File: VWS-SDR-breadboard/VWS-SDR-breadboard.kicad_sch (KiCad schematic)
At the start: 86 parts, among them J1 RF_IN, J3 Conn_01x14, U1 GALI-S66, U2 74CBTLV3253DR, U3 MC33078, U4 MC33078, U5 AMS1117-3.3

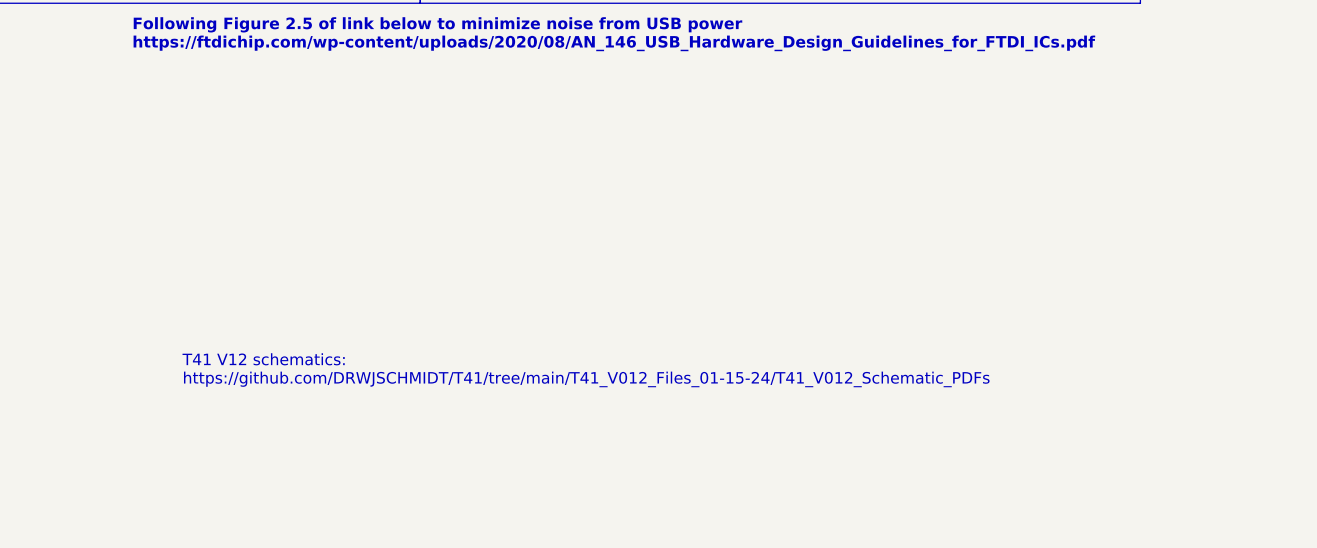
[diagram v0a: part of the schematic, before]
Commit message: Board cleanup; Updated schematic info block
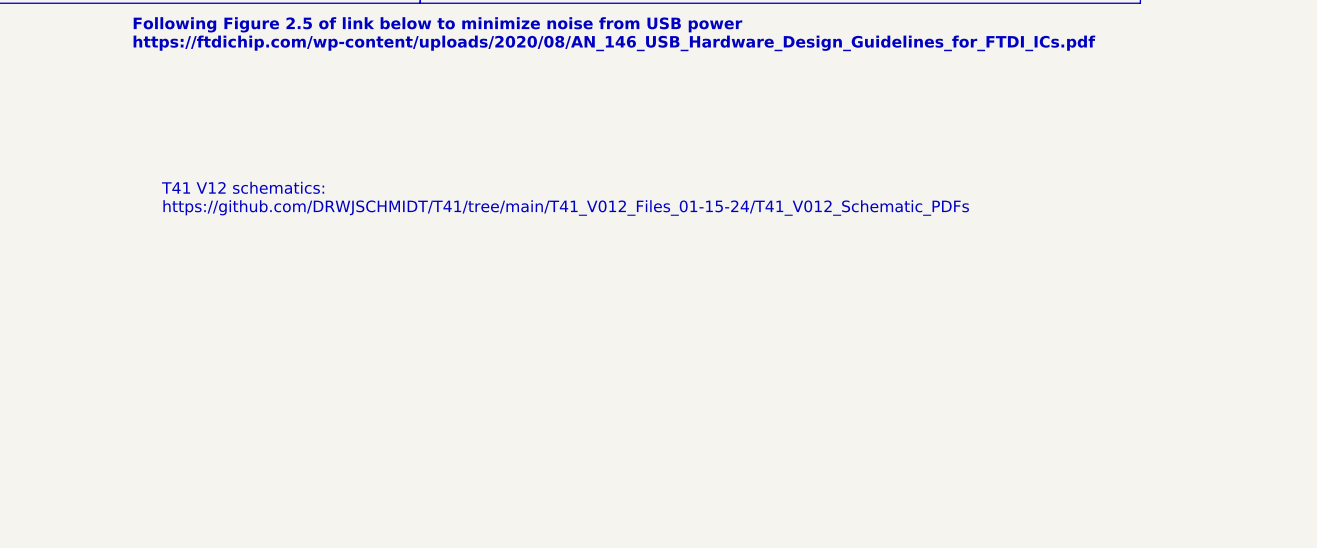
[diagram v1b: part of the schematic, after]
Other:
- title: VWS HF SDR -> VWS HF SDR frontend breadboard module
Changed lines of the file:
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@@
 	(paper "A4")
 	(title_block
-		(title "VWS HF SDR")
-		(date "2025-01-06")
-		(rev "V3")
+		(title "VWS HF SDR frontend breadboard module")
+		(date "2025-01-11")
+		(rev "V1.0")
 		(comment 1 "Heavily derived from T41 V12 RF board")
-		(comment 2 "Designed by Oliver KI3P")
+		(comment 2 "Original design by Oliver KI3P")
+		(comment 3 "Breadboard module version by Jacek KW4EP")
 	)
 	(junction
@@
 	(text "T41 V12 schematics:\nhttps://github.com/DRWJSCHMIDT/T41/tree/main/T41_V012_Files_01-15-24/T41_V012_Schematic_PDFs"
 		(exclude_from_sim no)
-		(at 178.054 169.164 0)
+		(at 175.768 150.114 0)
 		(effects
 			(font

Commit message: v1.1: - Changed order of pins on the connector to simplify routing. I/Q should be closer to the power pins. clock should be closer to the antenna - Added GND fill on the Vcc layer under the antenna trace to the breadboard connector -Added ground stitching around the RF amp
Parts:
- removed G1, G2, G5, G7: TestPoint, TestPoint:TestPoint_Pad_D2.0mm, symbol Connector:TestPoint
- removed H1, H2, H3, H4: ~, MountingHole:MountingHole_3.2mm_M3_DIN965_Pad, symbol Mechanical:MountingHole_Pad
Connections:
- net CLK0: now also J3.10 (Pin_10); no longer J3.6 (Pin_6)
- net CLK1: now also J3.11 (Pin_11); no longer J3.7 (Pin_7)
- net GND: now also J3.7 (Pin_7), J3.9 (Pin_9); no longer J3.10 (Pin_10), J3.8 (Pin_8)
- net I_out: now also J3.8 (Pin_8); no longer J3.9 (Pin_9)
- net Q_out: now also J3.6 (Pin_6); no longer J3.11 (Pin_11)
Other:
- note added: "Board revisions: v0.1 - Initial revision: removed clock gen abd pi board; Added pin connector v1.0 - Final design. 3.3v reg on board v1.1 - Removal of unpopulated components, signal on pin header rearranged for cleaner routing"
- note removed: "IQ out Ring - Q Tip - I"
- note removed: "Pico's 3.3V buck regulator supplies power for the Si5351 board and mixer"
- moved on the sheet: C27, C28, C29, C30, C31, L6, U5
